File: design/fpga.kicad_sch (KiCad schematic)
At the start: 83 parts, among them J7 DEBUG_FPGA_GPIO, J8 DIGILENT_JTAG_HS2_01X06, SW1 RST, SW2 PROG, U13 XC7S15-FTGB196, U14 IS25LP064A-JKx

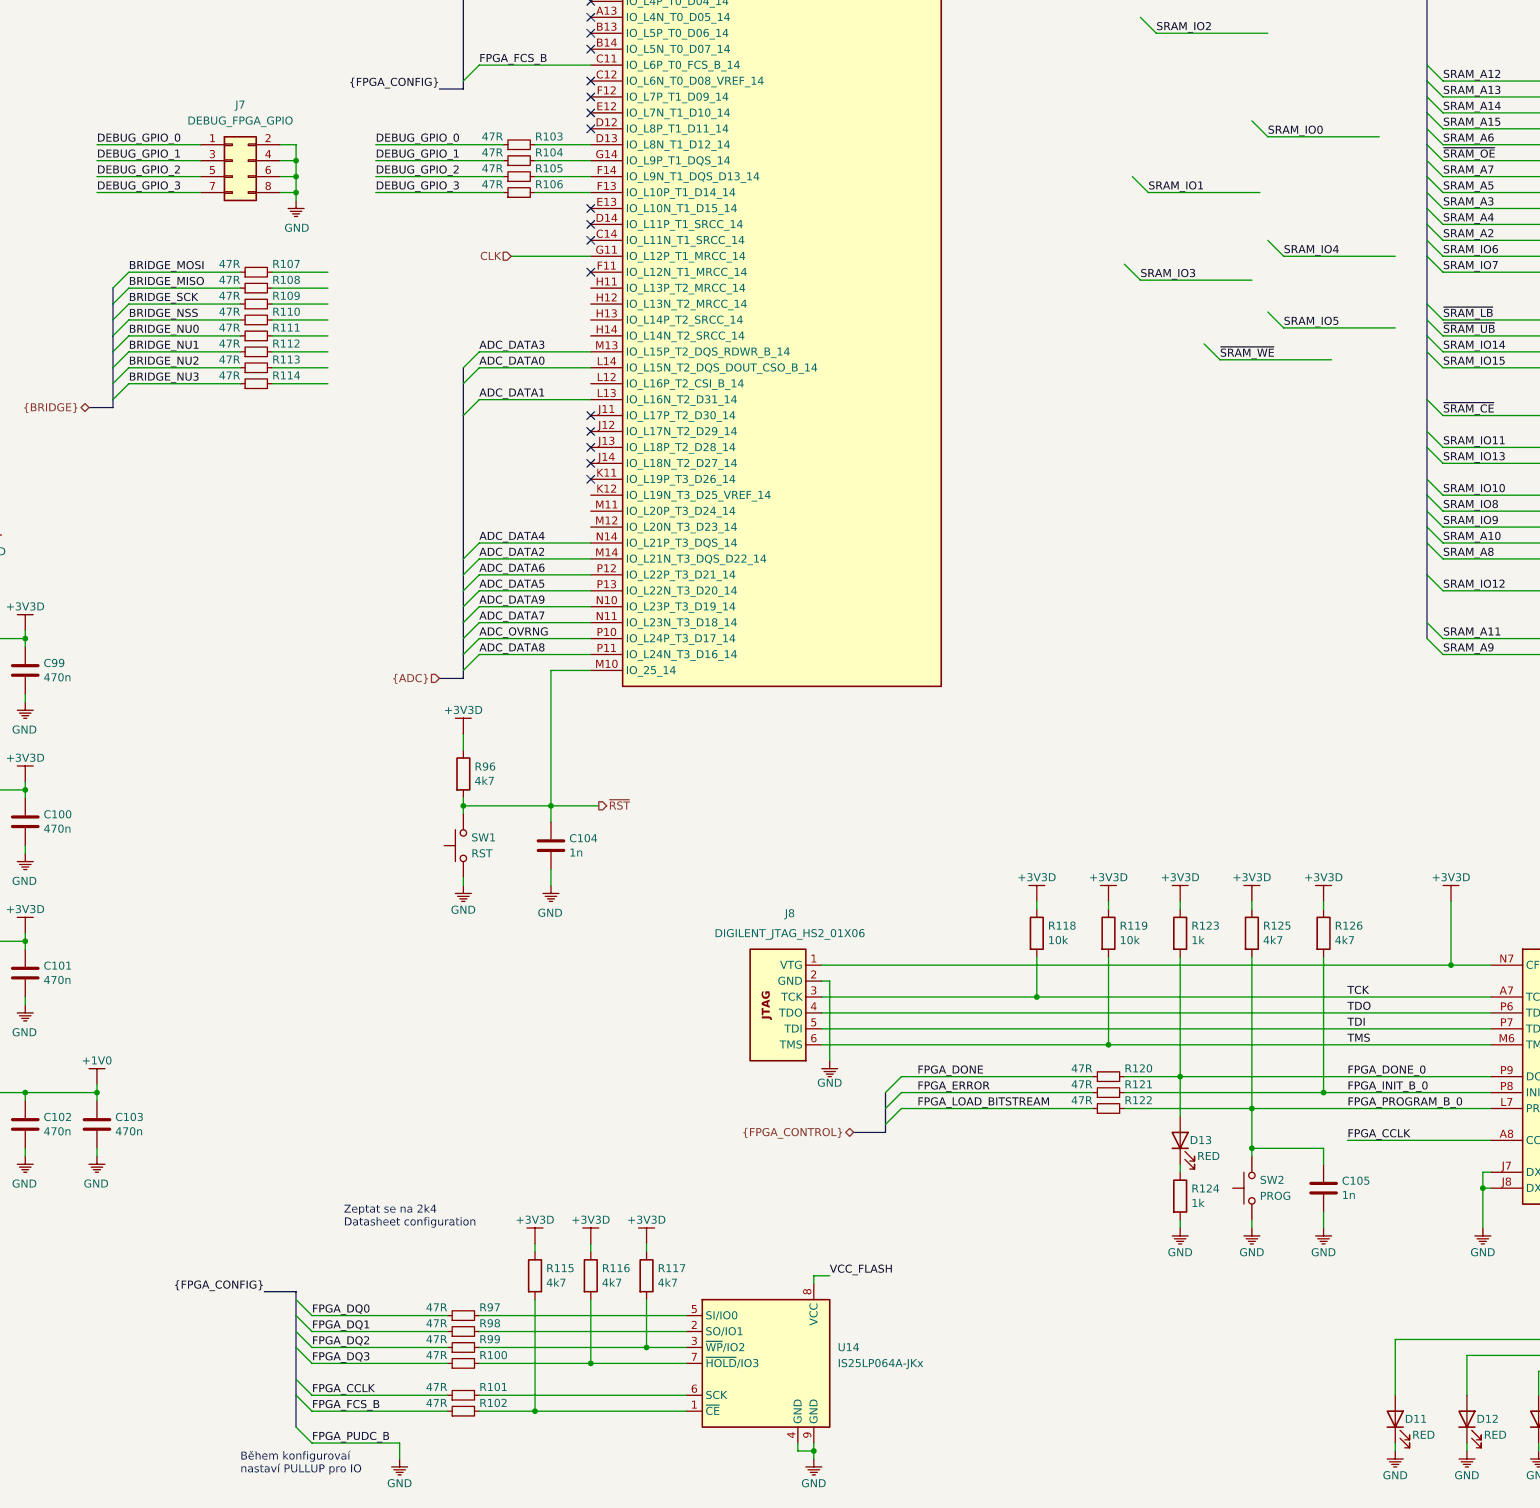
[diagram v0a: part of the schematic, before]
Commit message: Rename buses from X..0 to 0..X
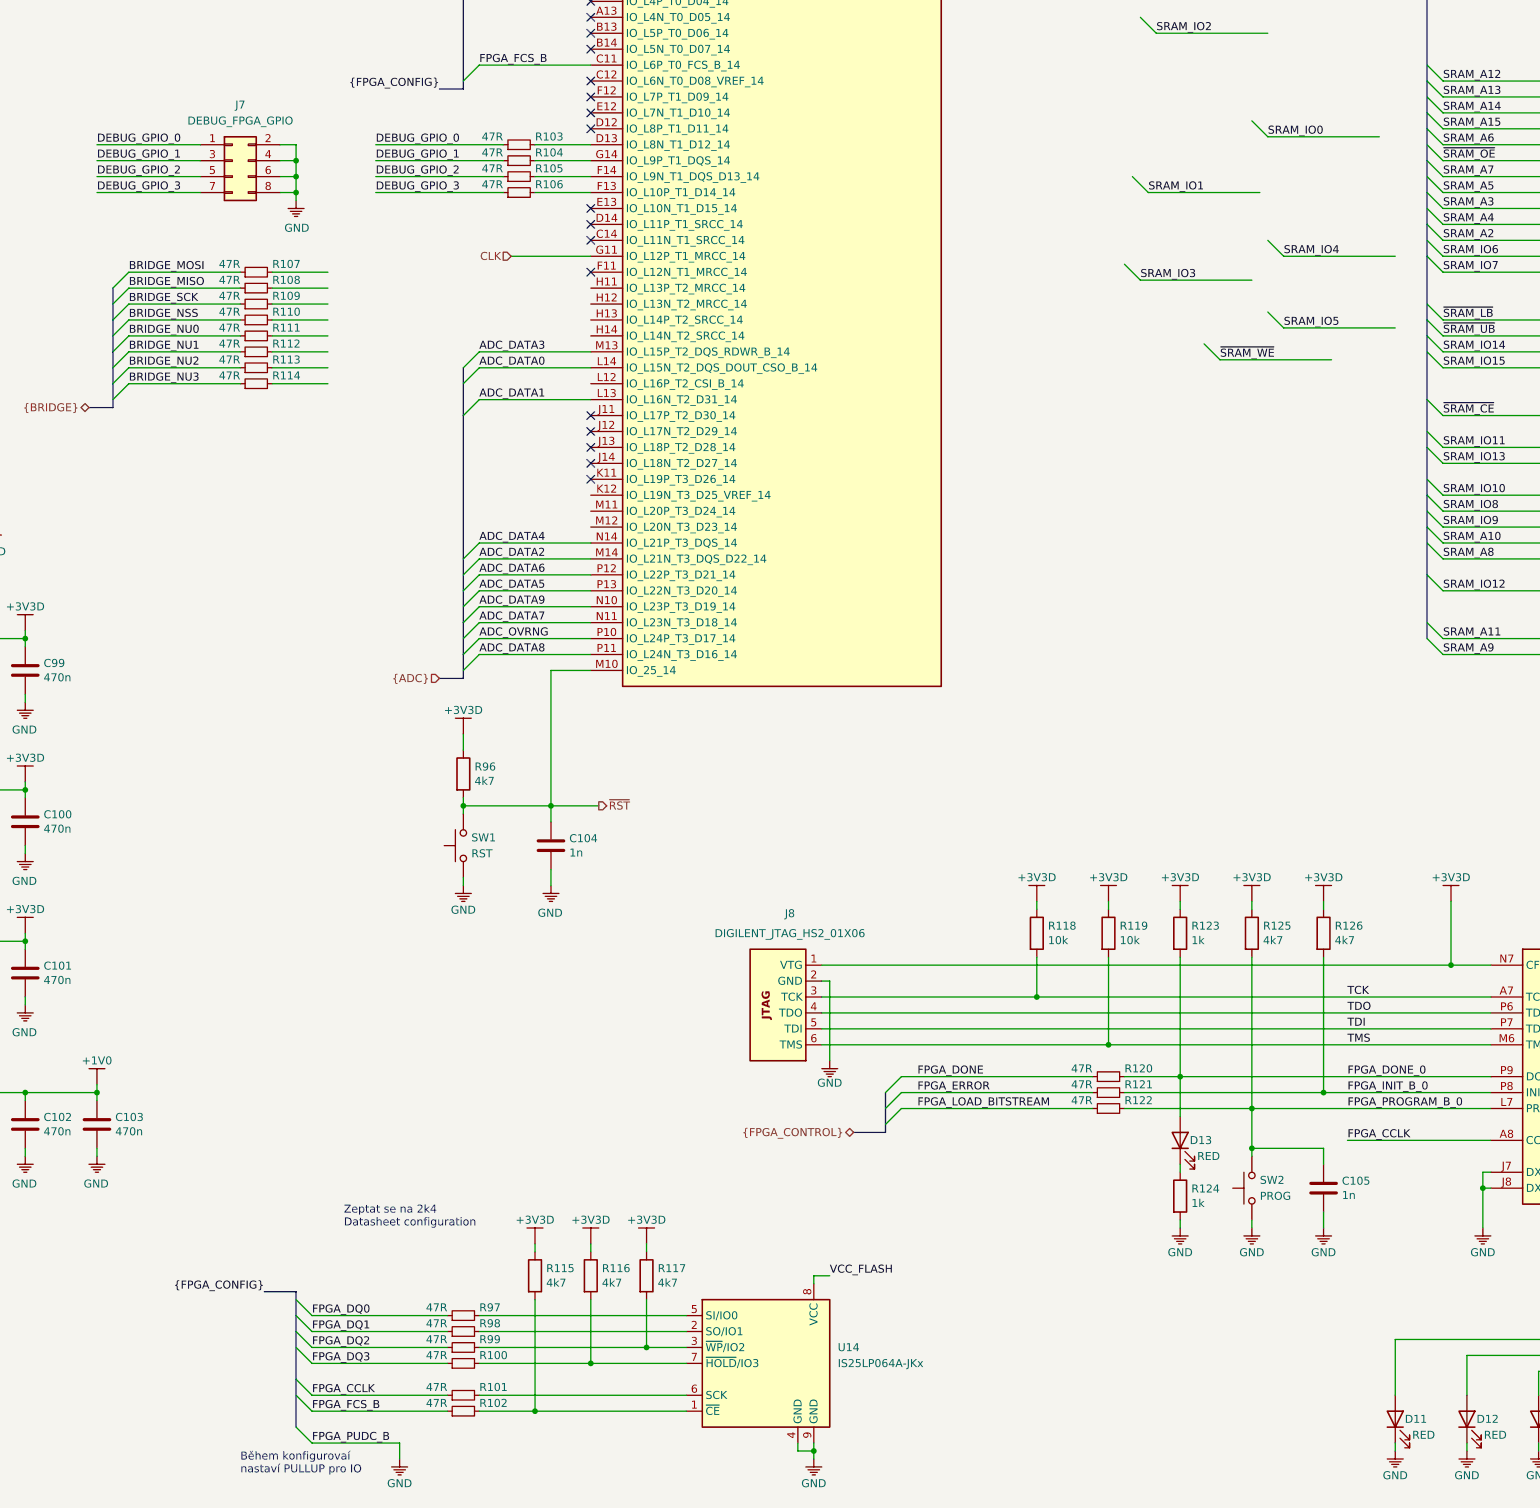
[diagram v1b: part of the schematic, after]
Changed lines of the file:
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@@
-(kicad_sch (version 20200506) (host eeschema "5.99.0-unknown-c3b50d3~101~ubuntu18.04.1")
-  (page "A3")
+(kicad_sch (version 20200512) (host eeschema "5.99.0-unknown-2cf82d9~101~ubuntu18.04.1")
+  (page 1 8)
+  (paper "A3")
   (title_block
     (title "Digitizer 10b 105 MSPS with FPGA")
@@
     (company "Jan Vykydal")
   )
+  (bus_alias "BRIDGE" (members "BRIDGE_MOSI" "BRIDGE_MISO" "BRIDGE_SCK" "BRIDGE_NSS" "BRIDGE_NU[0..3]"))
   (bus_alias "FPGA_CONTROL" (members "FPGA_DONE" "FPGA_ERROR" "FPGA_LOAD_BITSTREAM"))
-  (bus_alias "BRIDGE" (members "BRIDGE_MOSI" "BRIDGE_MISO" "BRIDGE_SCK" "BRIDGE_NSS" "BRIDGE_NU[3..0]"))
-  (bus_alias "FPGA_CONFIG" (members "FPGA_DQ[3..0]" "FPGA_CCLK" "FPGA_FCS_B" "FPGA_PUDC_B"))
+  (bus_alias "FPGA_CONFIG" (members "FPGA_DQ[0..3]" "FPGA_CCLK" "FPGA_FCS_B" "FPGA_PUDC_B"))
   (junction (at 26.67 26.67))
   (junction (at 26.67 29.21))
@@
   (junction (at 391.16 232.41))
   (junction (at 392.43 16.51))
-  (no_connect (at 185.42 58.42))
-  (no_connect (at 185.42 45.72))
+  (no_connect (at 185.42 86.36))
+  (no_connect (at 185.42 114.3))
+  (no_connect (at 185.42 50.8))
+  (no_connect (at 185.42 60.96))
   (no_connect (at 185.42 116.84))
-  (no_connect (at 185.42 50.8))
+  (no_connect (at 185.42 81.28))
+  (no_connect (at 185.42 40.64))
+  (no_connect (at 185.42 43.18))
+  (no_connect (at 185.42 48.26))
+  (no_connect (at 185.42 119.38))
   (no_connect (at 185.42 63.5))
   (no_connect (at 185.42 76.2))
-  (no_connect (at 185.42 48.26))
+  (no_connect (at 185.42 45.72))
+  (no_connect (at 185.42 111.76))
+  (no_connect (at 185.42 55.88))
+  (no_connect (at 185.42 78.74))
   (no_connect (at 185.42 109.22))
+  (no_connect (at 185.42 58.42))
   (no_connect (at 185.42 25.4))
-  (no_connect (at 185.42 78.74))
-  (no_connect (at 185.42 119.38))
-  (no_connect (at 185.42 81.28))
-  (no_connect (at 185.42 114.3))
-  (no_connect (at 185.42 86.36))
-  (no_connect (at 185.42 60.96))
-  (no_connect (at 185.42 111.76))
-  (no_connect (at 185.42 43.18))
-  (no_connect (at 185.42 55.88))
-  (no_connect (at 185.42 40.64))
   (bus_entry (at 109.22 88.9) (size 2.54 -2.54))
   (bus_entry (at 109.22 91.44) (size 2.54 -2.54))
@@
   (wire (pts (xy 392.43 16.51) (xy 394.97 16.51)))
   (bus (pts (xy 105.41 107.95) (xy 109.22 107.95)))
-  (bus (pts (xy 109.22 88.9) (xy 109.22 91.44)))
-  (bus (pts (xy 109.22 91.44) (xy 109.22 96.52)))
-  (bus (pts (xy 109.22 96.52) (xy 109.22 101.6)))
-  (bus (pts (xy 109.22 101.6) (xy 109.22 106.68)))
-  (bus (pts (xy 109.22 106.68) (xy 109.22 107.95)))
+  (bus (pts (xy 109.22 88.9) (xy 109.22 93.98)))
+  (bus (pts (xy 109.22 93.98) (xy 109.22 99.06)))
+  (bus (pts (xy 109.22 99.06) (xy 109.22 104.14)))
+  (bus (pts (xy 109.22 104.14) (xy 109.22 107.95)))
   (bus (pts (xy 133.35 248.92) (xy 138.43 248.92)))
   (bus (pts (xy 138.43 248.92) (xy 138.43 252.73)))
-  (bus (pts (xy 138.43 252.73) (xy 138.43 257.81)))
-  (bus (pts (xy 138.43 257.81) (xy 138.43 265.43)))
-  (bus (pts (xy 138.43 265.43) (xy 138.43 270.51)))
+  (bus (pts (xy 138.43 252.73) (xy 138.43 255.27)))
+  (bus (pts (xy 138.43 255.27) (xy 138.43 262.89)))
+  (bus (pts (xy 138.43 262.89) (xy 138.43 270.51)))
   (bus (pts (xy 161.29 57.15) (xy 165.1 57.15)))
   (bus (pts (xy 161.29 151.13) (xy 165.1 151.13)))
@@
   (bus (pts (xy 318.77 25.4) (xy 318.77 55.88)))
   (bus (pts (xy 318.77 55.88) (xy 318.77 60.96)))
-  (bus (pts (xy 318.77 60.96) (xy 318.77 66.04)))
-  (bus (pts (xy 318.77 66.04) (xy 318.77 71.12)))
-  (bus (pts (xy 318.77 71.12) (xy 318.77 76.2)))
-  (bus (pts (xy 318.77 76.2) (xy 318.77 78.74)))
+  (bus (pts (xy 318.77 60.96) (xy 318.77 63.5)))
+  (bus (pts (xy 318.77 63.5) (xy 318.77 68.58)))
+  (bus (pts (xy 318.77 68.58) (xy 318.77 73.66)))
+  (bus (pts (xy 318.77 73.66) (xy 318.77 78.74)))
   (bus (pts (xy 318.77 78.74) (xy 318.77 83.82)))
-  (bus (pts (xy 318.77 83.82) (xy 318.77 91.44)))
-  (bus (pts (xy 318.77 91.44) (xy 318.77 96.52)))
+  (bus (pts (xy 318.77 83.82) (xy 318.77 93.98)))
+  (bus (pts (xy 318.77 93.98) (xy 318.77 96.52)))
   (bus (pts (xy 318.77 96.52) (xy 318.77 106.68)))
   (bus (pts (xy 318.77 106.68) (xy 318.77 114.3)))
